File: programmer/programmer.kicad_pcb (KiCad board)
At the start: 2 copper layers, 14 x 30.5 mm, 5 parts, among them J1 Conn_01x05_Pin, J2 Conn_02x03_Odd_Even

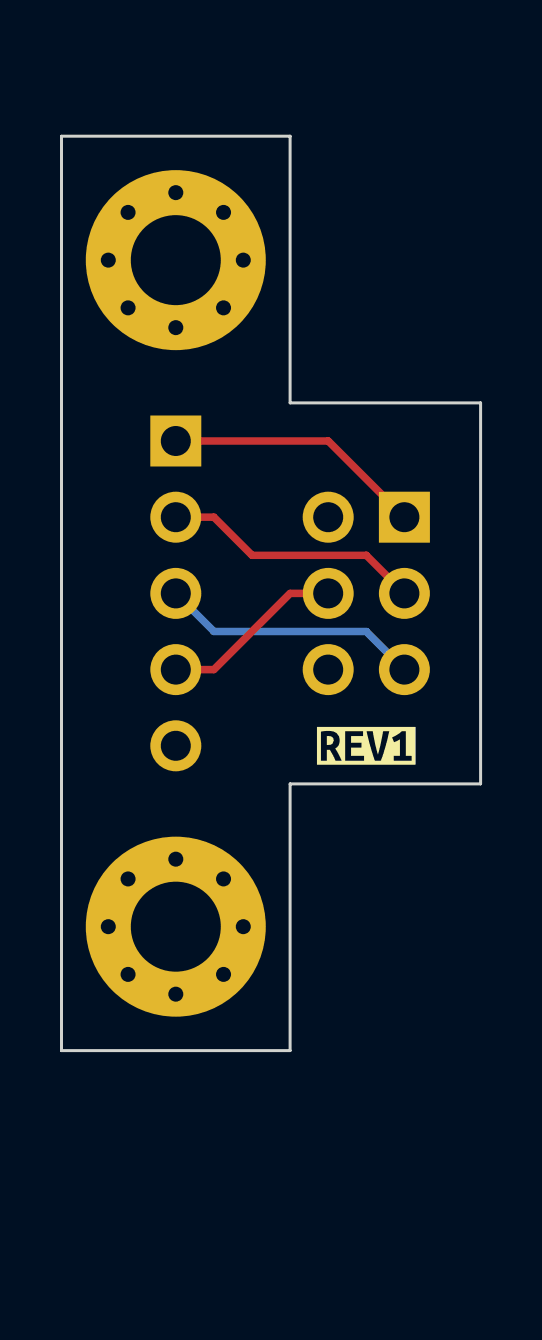
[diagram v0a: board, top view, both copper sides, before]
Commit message: update programming pcb so it can be secured to the stemma grid
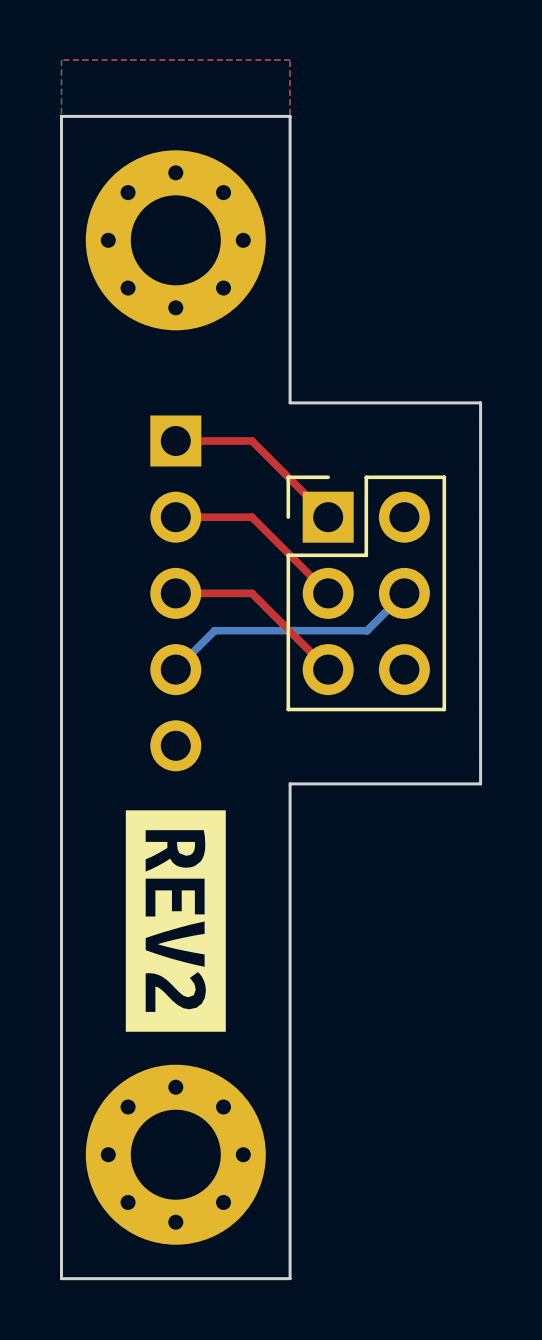
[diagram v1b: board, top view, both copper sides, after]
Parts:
- removed kibuzzard-64B22C68: G***, kibuzzard-64B22C68
- added kibuzzard-64ED132C: G***, kibuzzard-64ED132C, F.Cu at (137.2, 64.3)
- J2: moved to F.Cu
- moved H1 7.60 mm to (137.2, 72.1)
- moved J2 2.54 mm to (142.2, 50.8), turned to 0 degrees
- moved H2 0.66 mm to (137.2, 41.6)
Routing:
- net MISO: track 8.67 -> 6.13 mm
- net SCK: track 8.67 -> 6.13 mm
- net MOSI: track 6.13 -> 8.67 mm
- net RST: track 8.67 -> 6.13 mm
- added copper zone on F.Cu, net GND
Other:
- board size 14 x 30.5 mm -> 14 x 38.7 mm
